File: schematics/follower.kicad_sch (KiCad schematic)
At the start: 26 parts, among them M2 Motor, M3 Motor, Q1 TLE5206_2S, Q2 TLE5206_2S, SW5 Reset, U10 PIC32MX170F256B, U5 Tape_Left, U6 Tape_Middle, U7 Tape_Right, U8 Quadrature_Encoder, U9 Quadrature_Encoder

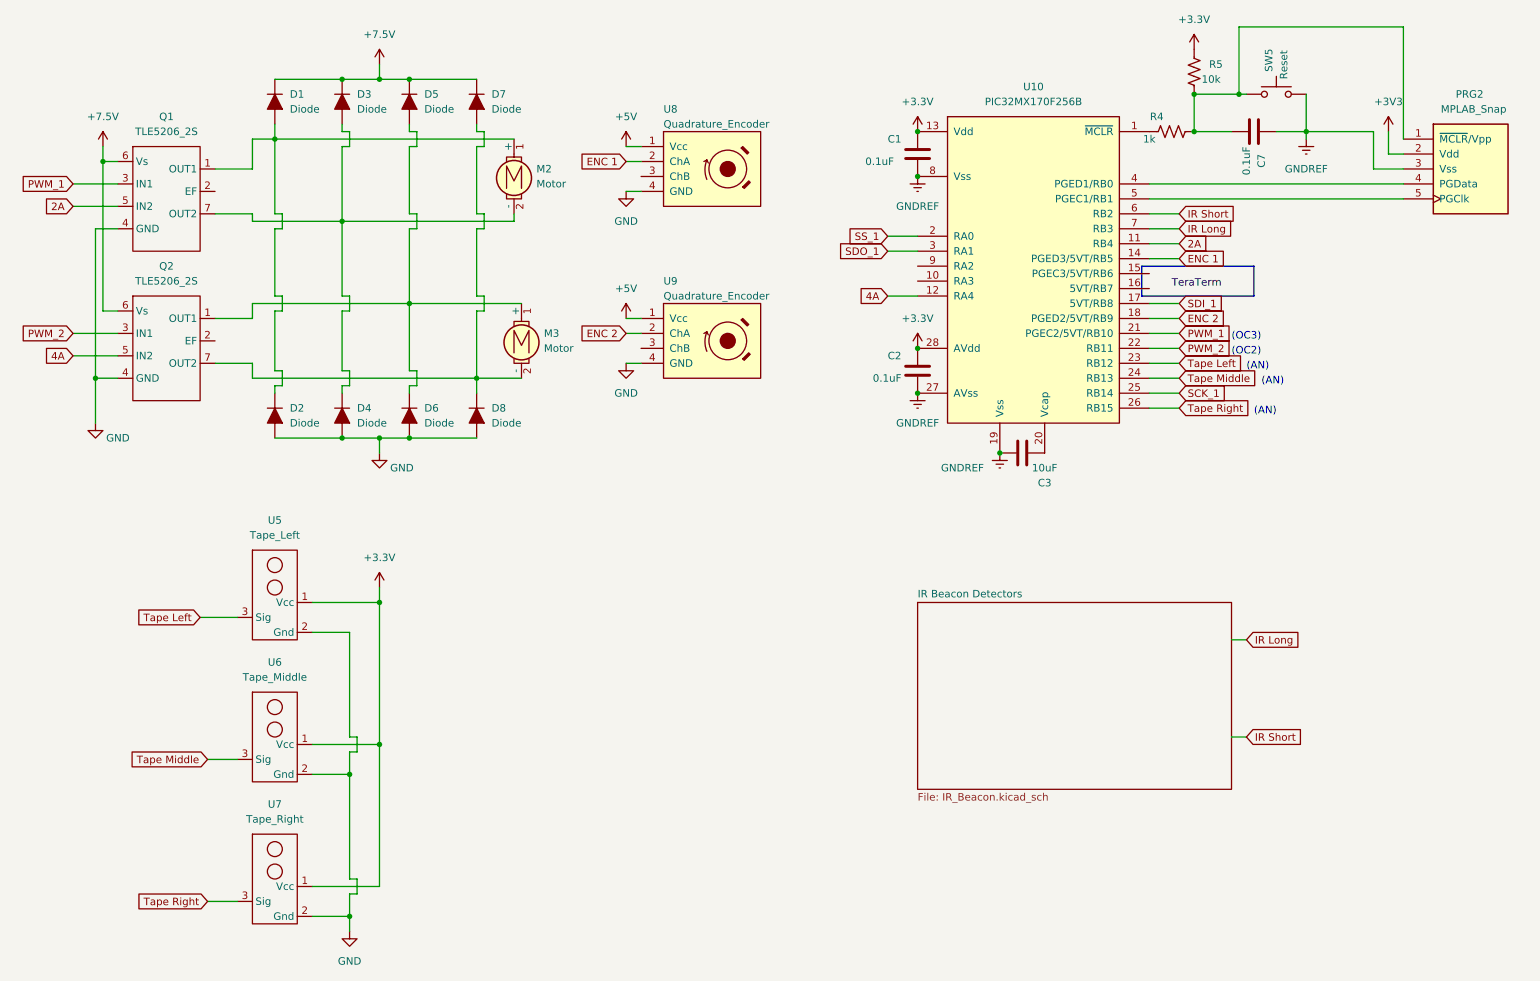
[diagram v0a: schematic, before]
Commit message: Gear SolidWorks files
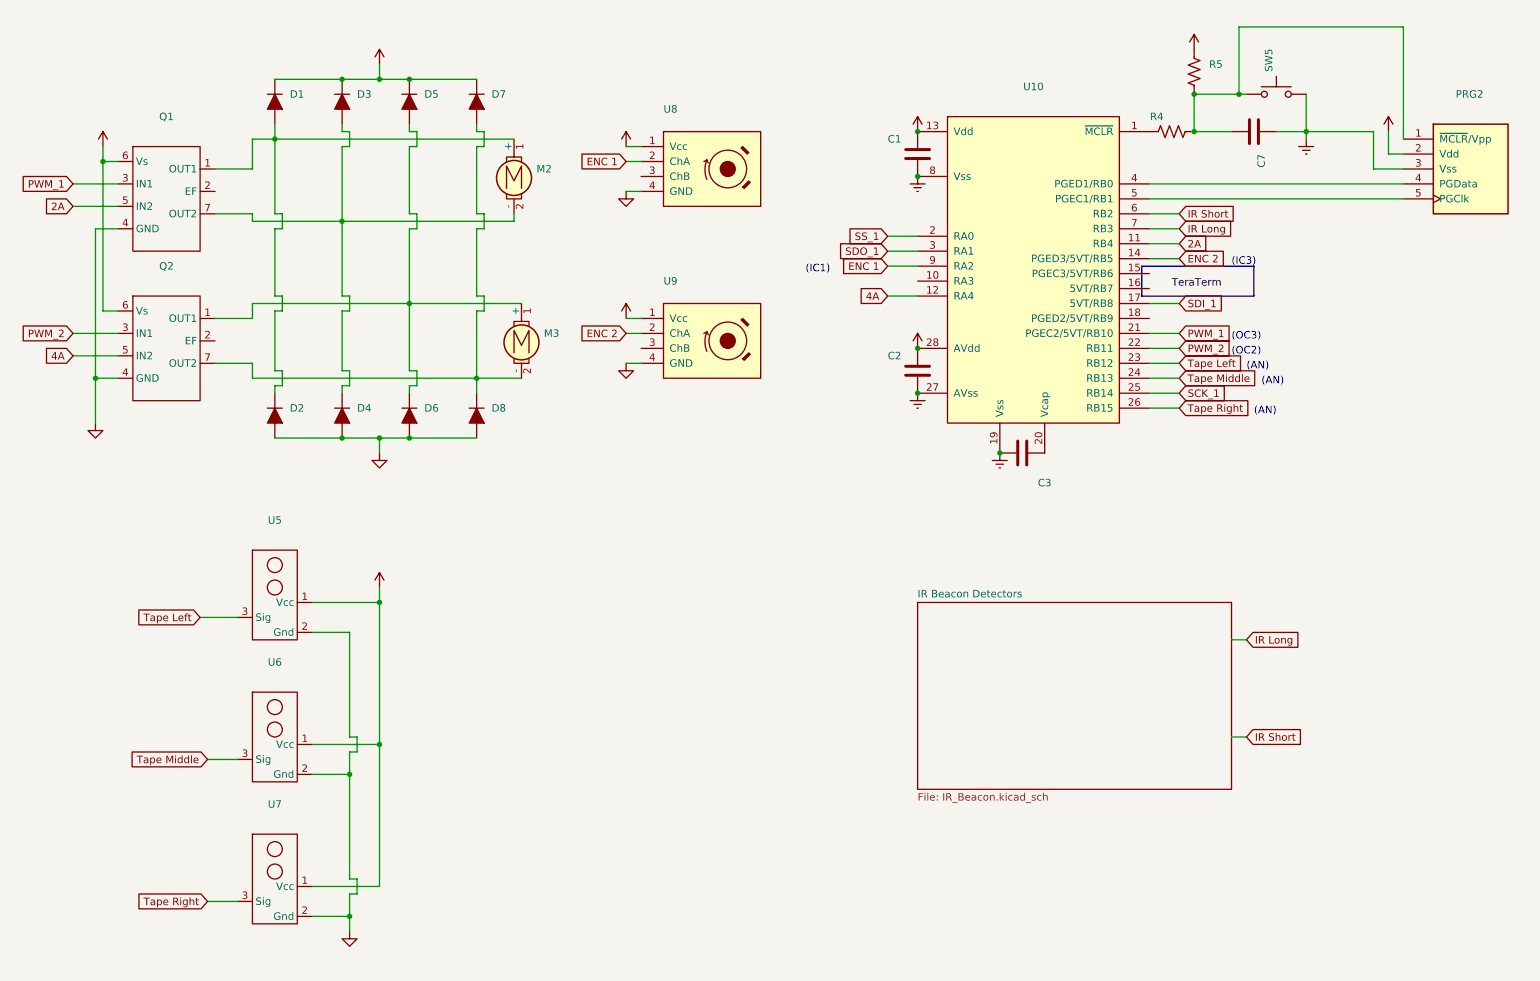
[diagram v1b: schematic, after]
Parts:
- C1, C2, C7: value 0.1uF -> (none)
- C3: value 10uF -> (none)
- D1, D2, D3, D4, D5, D6, D7, D8: value Diode -> (none)
- M2, M3: value Motor -> (none)
- PRG2: value MPLAB_Snap -> (none)
- Q1, Q2: value TLE5206_2S -> (none)
- R4: value 1k -> (none)
- R5: value 10k -> (none)
- SW5: value Reset -> (none)
- U10: value PIC32MX170F256B -> (none)
- U5: value Tape_Left -> (none)
- U6: value Tape_Middle -> (none)
- U7: value Tape_Right -> (none)
- U8, U9: value Quadrature_Encoder -> (none)
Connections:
- net ENC 1: now also U10.9 (RA2); no longer U10.14 (PGED3/5VT/RB5)
- net ENC 2: now also U10.14 (PGED3/5VT/RB5); no longer U10.18 (PGED2/5VT/RB9)
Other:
- note added: "(IC1)"
- note added: "(IC3)"
